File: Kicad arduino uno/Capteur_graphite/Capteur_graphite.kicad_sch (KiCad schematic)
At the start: 21 parts, among them J1 Power, J2 Digital/PWM, J3 Analog, J4 Digital/PWM, U3 MCP41050, U4 LTC1050

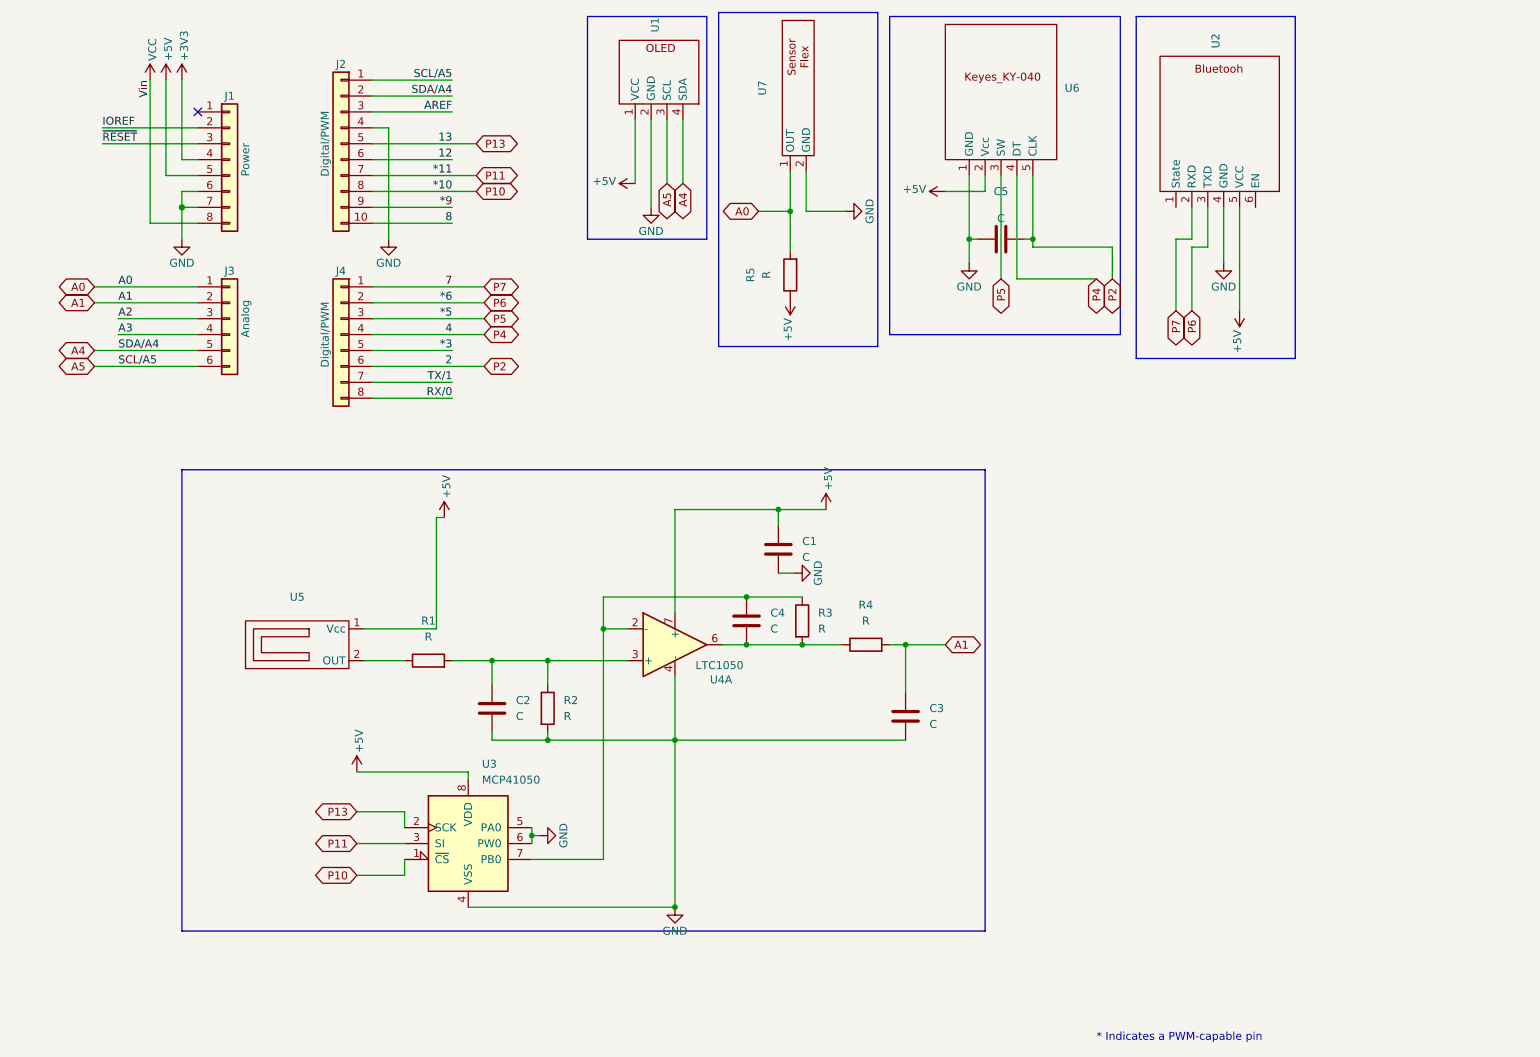
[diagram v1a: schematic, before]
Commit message: Save_sans_via_mais_avec_modif_pin
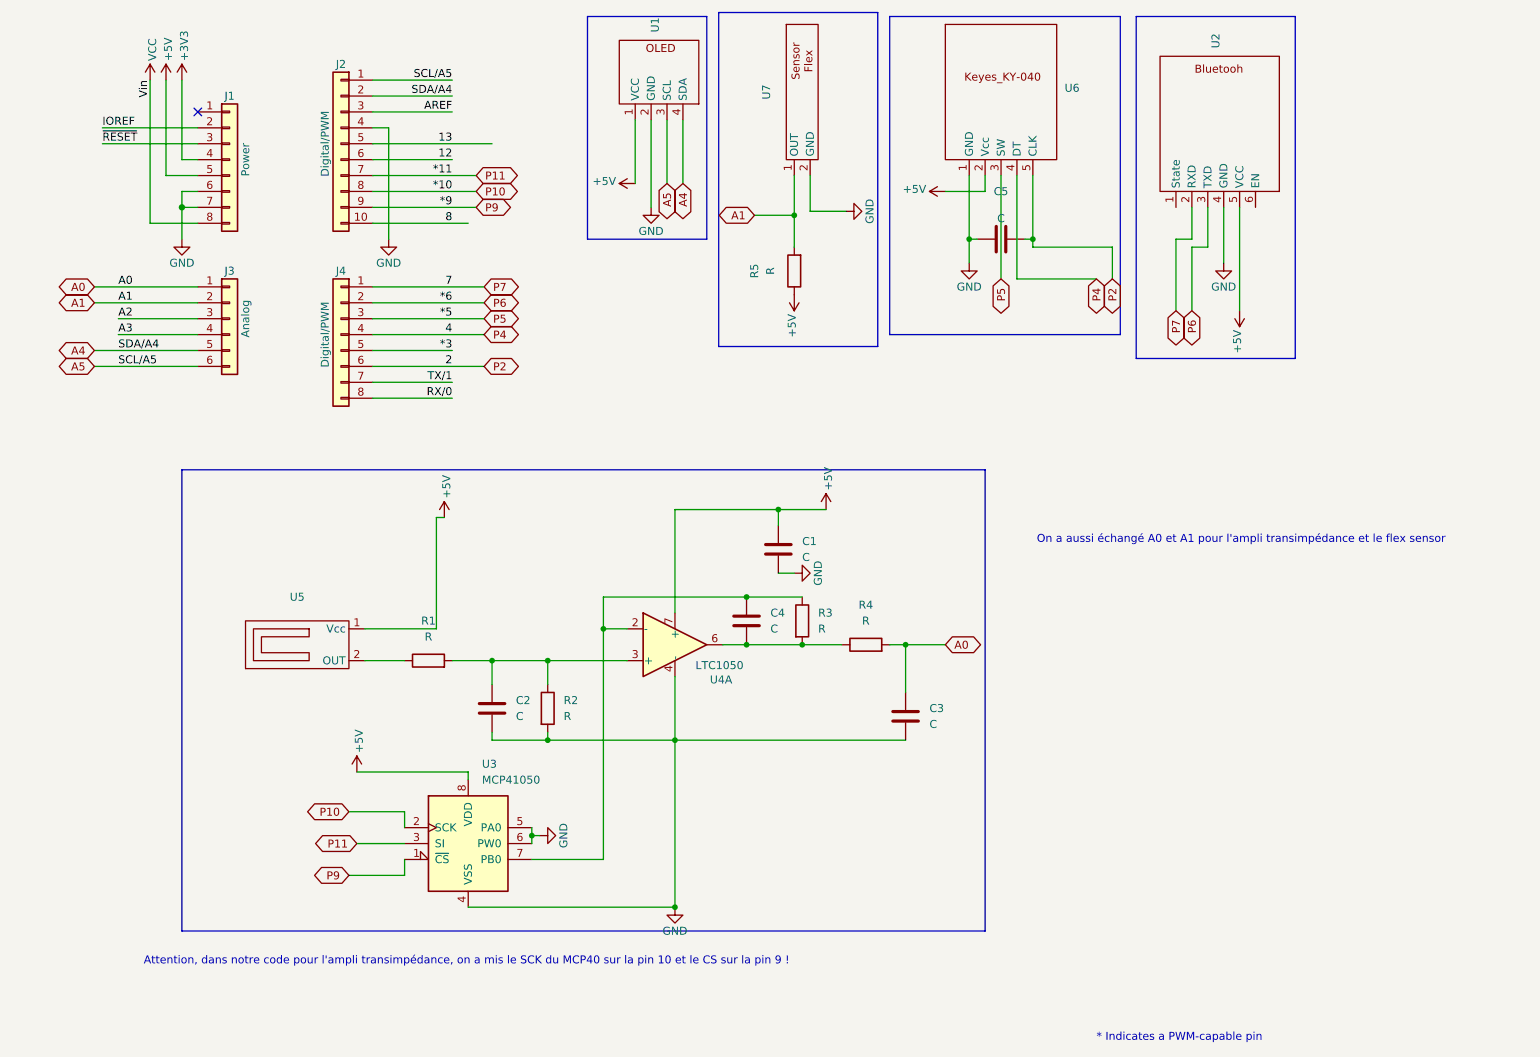
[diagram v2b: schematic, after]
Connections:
- net A0: now also C3.2, R4.2; no longer R5.2, U7.1 (OUT)
- net A1: now also R5.2, U7.1 (OUT); no longer C3.2, R4.2
- net P10: now also U3.2 (SCK); no longer U3.1 (~{CS})
- net *9 renamed P9
- net P9: now also U3.1 (~{CS})
- net P13 renamed 13
- net 13: no longer U3.2 (SCK)
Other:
- note added: "Attention, dans notre code pour l'ampli transimpédance, on a mis le SCK du MCP40 sur la pin 10 et le CS sur la pin 9 !"
- note added: "On a aussi échangé A0 et A1 pour l'ampli transimpédance et le flex sensor"
- moved on the sheet: R5, U7

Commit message: sans_via_mais_bonne_modif_pin_(SCK_sur_la_13)
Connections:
- net 13 renamed P13
- net P13: now also U3.2 (SCK)
- net P10 renamed *10
- net *10: no longer U3.2 (SCK)
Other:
- note added: "Attention, dans notre code pour l'ampli transimpédance, on a mis le CS sur la pin 9 !"
- note removed: "Attention, dans notre code pour l'ampli transimpédance, on a mis le SCK du MCP40 sur la pin 10 et le CS sur la pin 9 !"
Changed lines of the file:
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@@
 	(wire
 		(pts
-			(xy 81.28 36.83) (xy 62.23 36.83)
+			(xy 62.23 36.83) (xy 82.55 36.83)
 		)
 		(stroke
@@
 	(wire
 		(pts
-			(xy 62.23 44.45) (xy 78.74 44.45)
-		)
-		(stroke
-			(width 0)
-			(type solid)
-		)
-	)
-	(wire
-		(pts
 			(xy 130.81 116.84) (xy 137.16 116.84)
 		)
@@
 	(wire
 		(pts
+			(xy 83.82 44.45) (xy 62.23 44.45)
+		)
+		(stroke
+			(width 0)
+			(type solid)
+		)
+	)
+	(wire
+		(pts
 			(xy 77.47 49.53) (xy 62.23 49.53)
 		)
@@
 		(pts
 			(xy 62.23 46.99) (xy 78.74 46.99)
+		)
+		(stroke
+			(width 0)
+			(type solid)
+		)
+	)
+	(wire
+		(pts
+			(xy 85.09 45.72) (xy 83.82 45.72)
 		)
 		(stroke
@@
 		)
 	)
-	(text "Attention, dans notre code pour l'ampli transimpédance, on a mis le SCK du MCP40 sur la pin 10 et le CS sur la pin 9 !\n"
+	(text "Attention, dans notre code pour l'ampli transimpédance, on a mis le CS sur la pin 9 !\n"
 		(exclude_from_sim no)
 		(at 77.216 167.386 0)
@@
 		)
 	)
-	(global_label "P10"
+	(global_label "P13"
 		(shape bidirectional)
-		(at 78.74 44.45 0)
+		(at 82.55 36.83 0)
 		(fields_autoplaced yes)
 		(effects
@@
 		)
 		(property "Intersheetrefs" "${INTERSHEET_REFS}"
-			(at 86.5253 44.45 0)
+			(at 90.3353 36.83 0)
 			(effects
 				(font
@@
 		)
 	)
-	(global_label "P10"
+	(global_label "P13"
 		(shape bidirectional)
 		(at 58.42 143.51 180)

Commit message: soft_ware_beginning
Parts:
- C1: value C -> 1pf
- C2, C3: value C -> 100nf
- C4: value C -> 0.1µf
- C5: value C -> 100n
- R1: value R -> 10k
- R2, R3: value R -> 100k
- R4: value R -> 1k
- R5: value R -> 47k
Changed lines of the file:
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@@
 	(wire
 		(pts
-			(xy 85.09 45.72) (xy 83.82 45.72)
-		)
-		(stroke
-			(width 0)
-			(type solid)
-		)
-	)
-	(wire
-		(pts
 			(xy 121.92 109.22) (xy 130.81 109.22)
 		)
@@
 			)
 		)
-		(property "Value" "R"
+		(property "Value" "100k"
 			(at 92.71 128.2699 0)
 			(effects
@@
 			)
 		)
-		(property "Value" "R"
+		(property "Value" "100k"
 			(at 133.35 114.2999 0)
 			(effects
@@
 			)
 		)
-		(property "Value" "R"
+		(property "Value" "10k"
 			(at 71.12 115.57 90)
 			(effects
@@
 			)
 		)
-		(property "Value" "C"
+		(property "Value" "1pf"
 			(at 130.81 102.8699 0)
 			(effects
@@
 			)
 		)
-		(property "Value" "C"
+		(property "Value" "100nf"
 			(at 151.13 129.5399 0)
 			(effects
@@
 			)
 		)
-		(property "Value" "C"
+		(property "Value" "100nf"
 			(at 85.09 128.2699 0)
 			(effects
@@
 			)
 		)
-		(property "Value" "C"
+		(property "Value" "0.1µf"
 			(at 125.73 114.2999 0)
 			(effects
@@
 		(fields_autoplaced yes)
 		(property "Reference" "R5"
-			(at 123.19 57.15 90)
+			(at 132.08 55.8799 0)
 			(effects
 				(font
 					(size 1.27 1.27)
 				)
+				(justify right)
 			)
 		)
-		(property "Value" "R"
-			(at 125.73 57.15 90)
+		(property "Value" "47k"
+			(at 132.08 58.4199 0)
 			(effects
 				(font
 					(size 1.27 1.27)
 				)
+				(justify right)
 			)
 		)
@@
 			)
 		)
-		(property "Value" "C"
+		(property "Value" "100n"
 			(at 162.56 48.768 90)
 			(effects
@@
 			)
 		)
-		(property "Value" "R"
+		(property "Value" "1k"
 			(at 140.97 113.03 90)
 			(effects
